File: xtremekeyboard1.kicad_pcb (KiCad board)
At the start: 2 copper layers, 147 x 125.1 mm, 77 parts, among them J2 Conn_01x05_Pin, J3 Conn_01x05_Socket, SW1 1u MX, SW10 1u MX, SW11 1u MX, SW12 1u MX, SW13 1u MX, SW14 1u MX, SW15 1u MX, SW16 1u MX, SW17 1u MX, SW18 1u MX, SW19 1u MX, SW2 1u MX, SW20 1u MX, SW21 1u MX, SW22 1u MX, SW23 1u MX, SW24 1u MX, SW25 1u MX, SW26 1u MX, SW27 1u MX, SW3 1u MX, SW4 1u MX, SW5 1u MX, SW6 1u MX, SW7 1u MX, SW8 1u MX, SW9 1u MX, U1 rp2040-zero, U2 PS4 Joystick

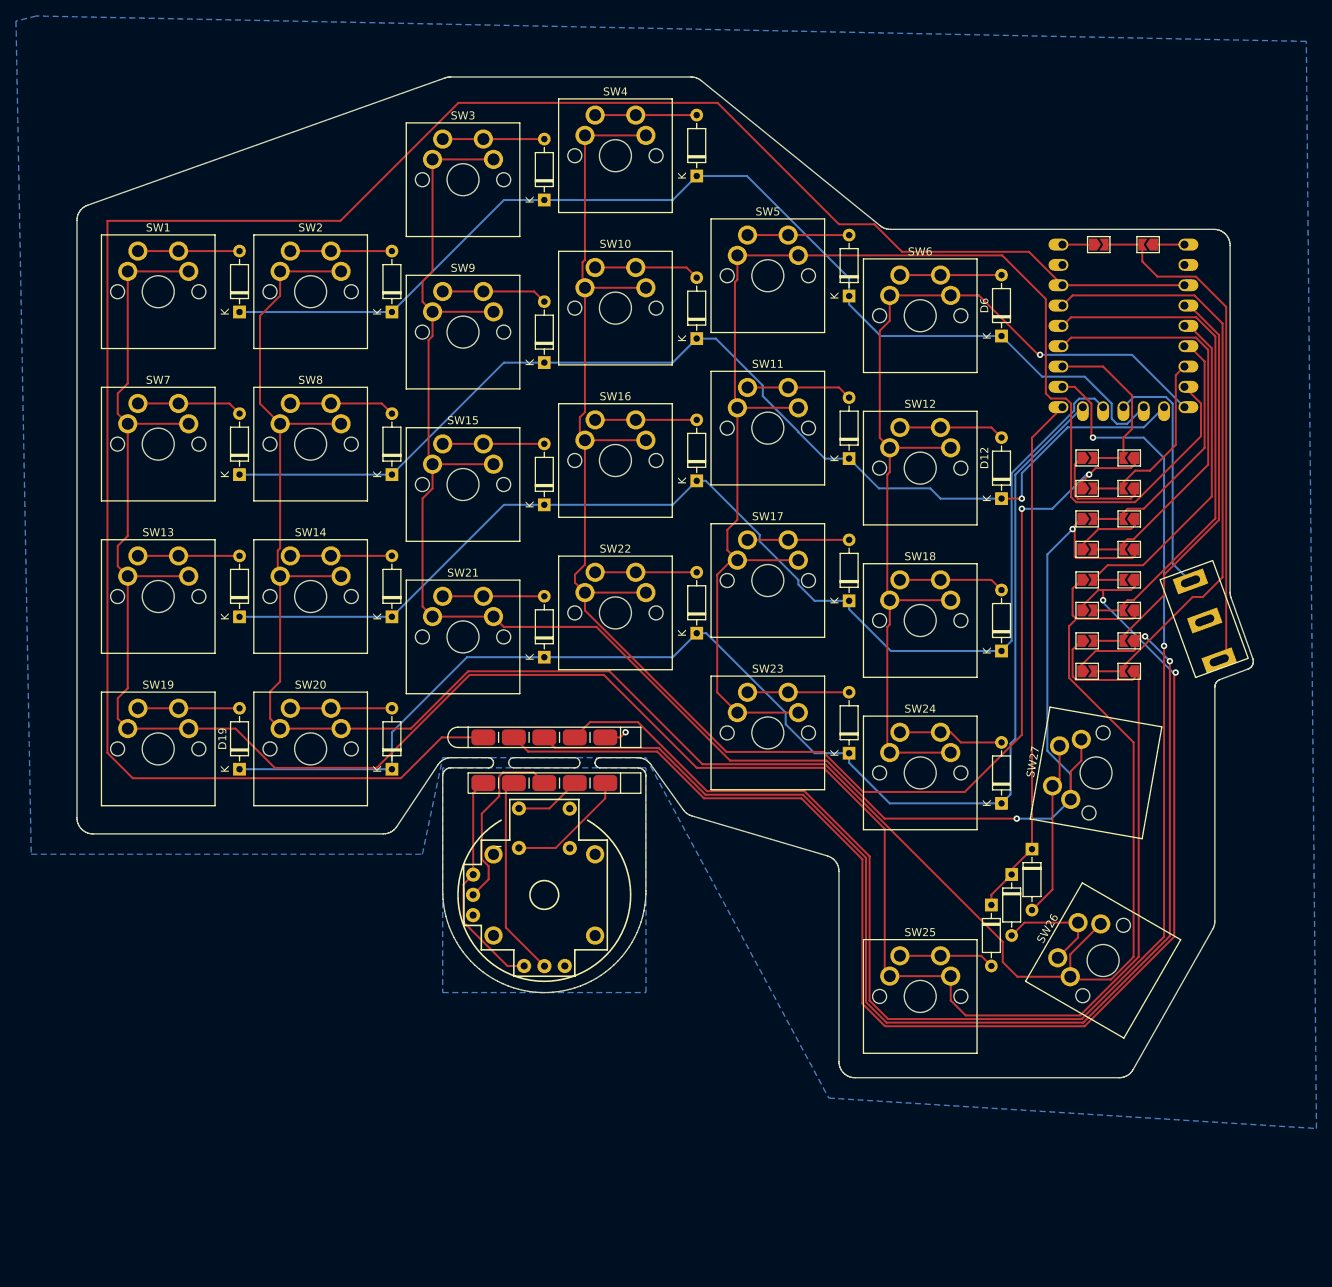
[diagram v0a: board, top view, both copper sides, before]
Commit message: finished pcb routing
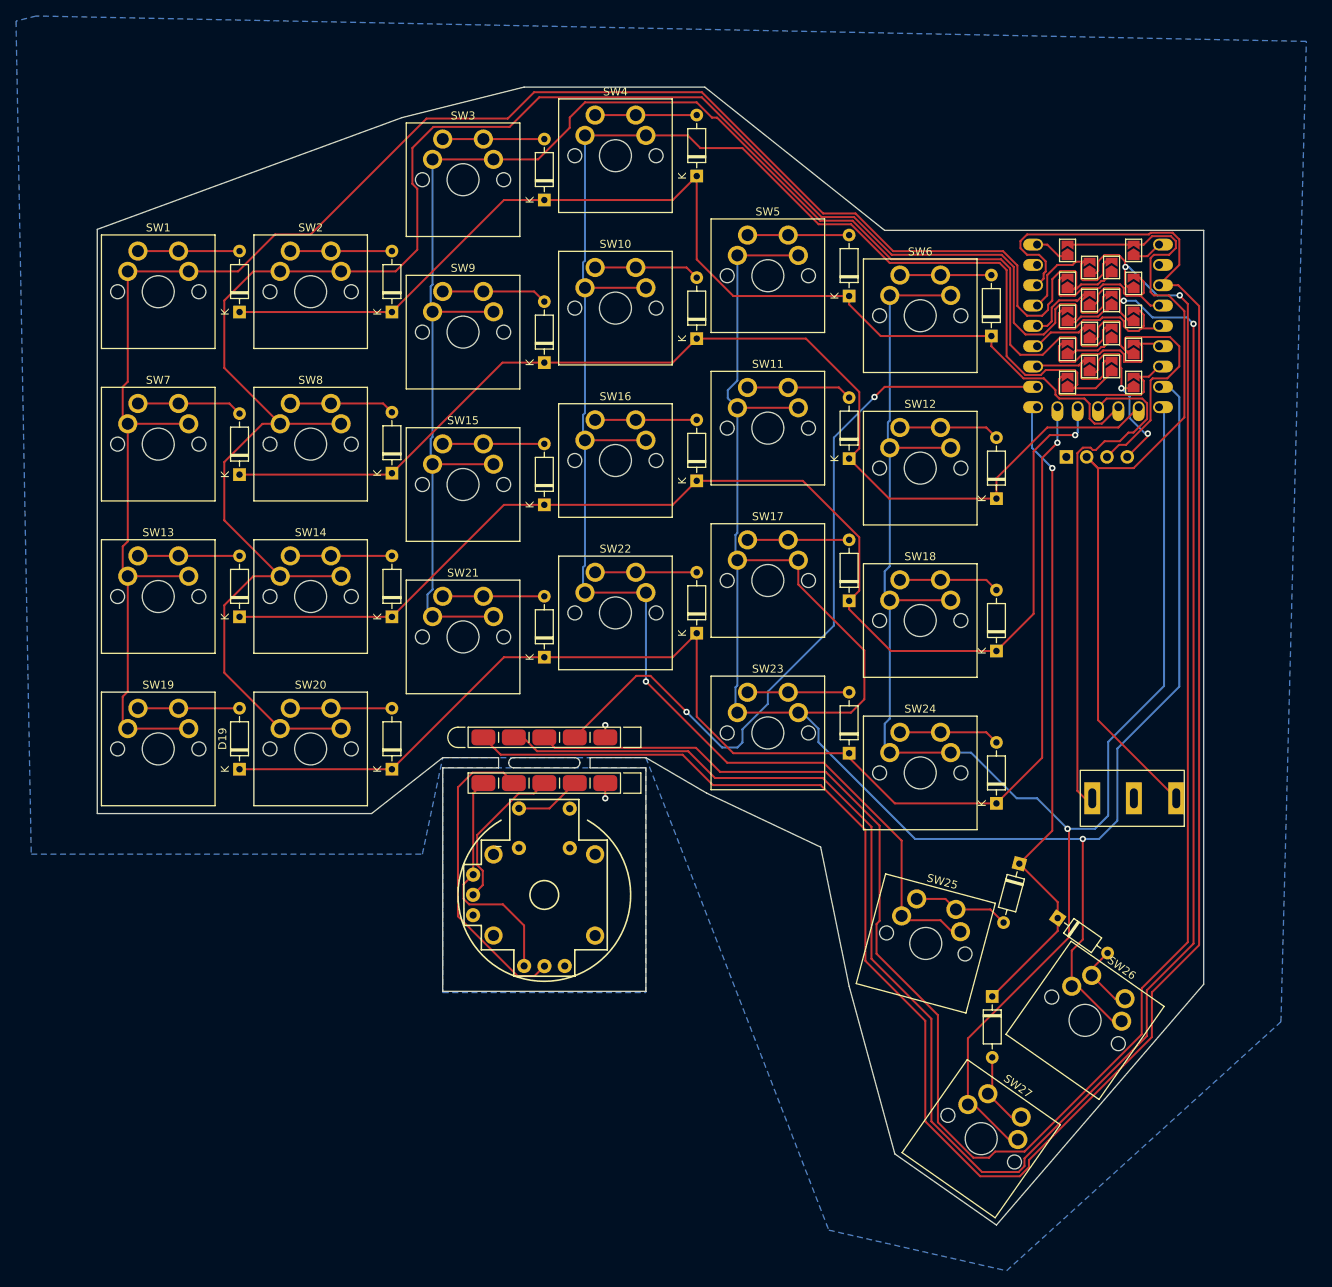
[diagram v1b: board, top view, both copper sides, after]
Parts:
- added J4: OLED-128x32, display:OLED-128x32-cutout, F.Cu at (180.5, 74.5)
- moved JP5 50.5 mm to (176.3, 52.4), turned to 90 degrees
- moved JP4 50.5 mm to (173.6, 52.4), turned to 90 degrees
- moved SW27 47.9 mm to (160.0, 161.3), turned to -35 degrees
- moved JP6 44.7 mm to (170.8, 54.4), turned to 90 degrees
- moved JP3 44.7 mm to (179.1, 54.4), turned to 90 degrees
- moved JP9 38.8 mm to (176.3, 56.5), turned to 90 degrees
- moved JP8 38.7 mm to (173.6, 56.5), turned to 90 degrees
- moved JP10 33.0 mm to (170.8, 58.5), turned to 90 degrees
- moved JP7 32.9 mm to (179.1, 58.5), turned to 90 degrees
- moved JP13 27.1 mm to (176.3, 60.6), turned to 90 degrees
- moved JP12 27.0 mm to (173.6, 60.6), turned to 90 degrees
- moved J1 23.8 mm to (179.2, 118.7), turned to -90 degrees
- moved JP14 21.3 mm to (170.8, 62.6), turned to 90 degrees
- moved JP11 21.2 mm to (179.1, 62.6), turned to 90 degrees
- moved D27 19.1 mm to (161.4, 143.5)
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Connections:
- SW25 pad 1: /COL0 -> /COL3
- SW26 pad 1: /COL1 -> /COL4
- SW27 pad 1: /COL2 -> /COL5
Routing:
- net /COL5: track 124.2 -> 215.2 mm
- net /JOYSW: track 183.2 -> 99.0 mm
- net /JOYY: track 157.6 -> 234.7 mm
- net /COL4: track 178.7 -> 253.4 mm, vias 0 -> 1
- net /JOYX: track 169.0 -> 238.9 mm
- net /COL0: track 298.8 -> 237.6 mm
- net /JYa: track 75.2 -> 18.9 mm
- net /JXa: track 63.8 -> 17.5 mm
- net +5V: track 64.2 -> 103.6 mm
- net /COL2: track 232.1 -> 193.4 mm, vias 2 -> 0
- net /SCLa: track 52.9 -> 15.3 mm
- net /TX: track 30.2 -> 63.1 mm
- net /COL1: track 279.5 -> 247.6 mm
- net /COL3: track 207.5 -> 239.4 mm, vias 2 -> 1
- net /JYb: track 52.8 -> 21.0 mm
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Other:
- board size 147 x 125.1 mm -> 138.3 x 142.2 mm

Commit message: finished good pcb, need to make oled reversible, maybe put jumpers on respective side
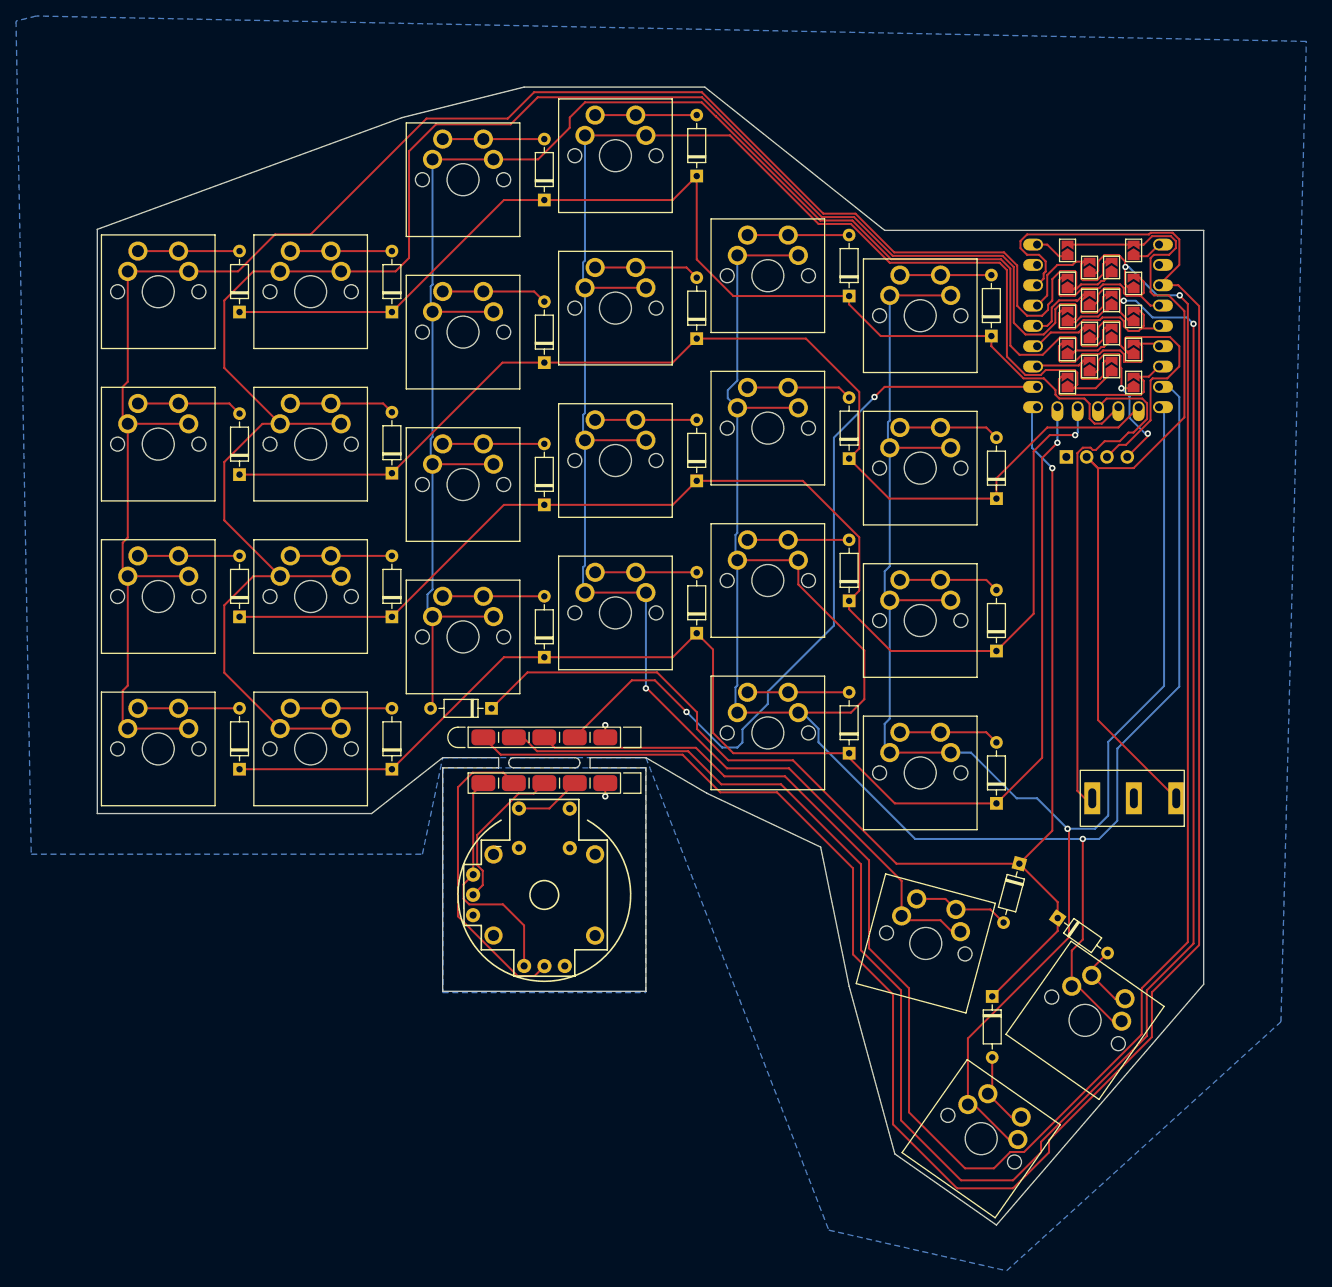
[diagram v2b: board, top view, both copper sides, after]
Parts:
- added D28: 1N4148, Diode_THT:D_DO-35_SOD27_P7.62mm_Horizontal, F.Cu at (98.8, 107.5)
- SW1, SW10, SW11, SW12, SW13, SW14, SW15, SW16, SW17, SW18, SW19, SW2, SW20, SW21, SW22, SW23, SW24, SW25, SW26, SW27, SW3, SW4, SW5, SW6, SW7, SW8, SW9: footprint PCM_Switch_Keyboard_Cherry_MX:SW_Cherry_MX_PCB_1.00u -> PCM_Switch_Keyboard_Cherry_MX:MX_PCB_Reversible
- U1: footprint keyboard_mcu:rp2040-zero-tht -> mcu:rp2040-zero-tht
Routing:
- net /ROW4: track 82.1 -> 161.0 mm
- net /COL2: track 193.4 -> 205.1 mm
- net /COL3: track 239.4 -> 236.9 mm
- net /JOYY: track 234.7 -> 233.5 mm
- net /COL1: track 247.6 -> 247.1 mm

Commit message: added pullup resistors, fixed solder jumpers
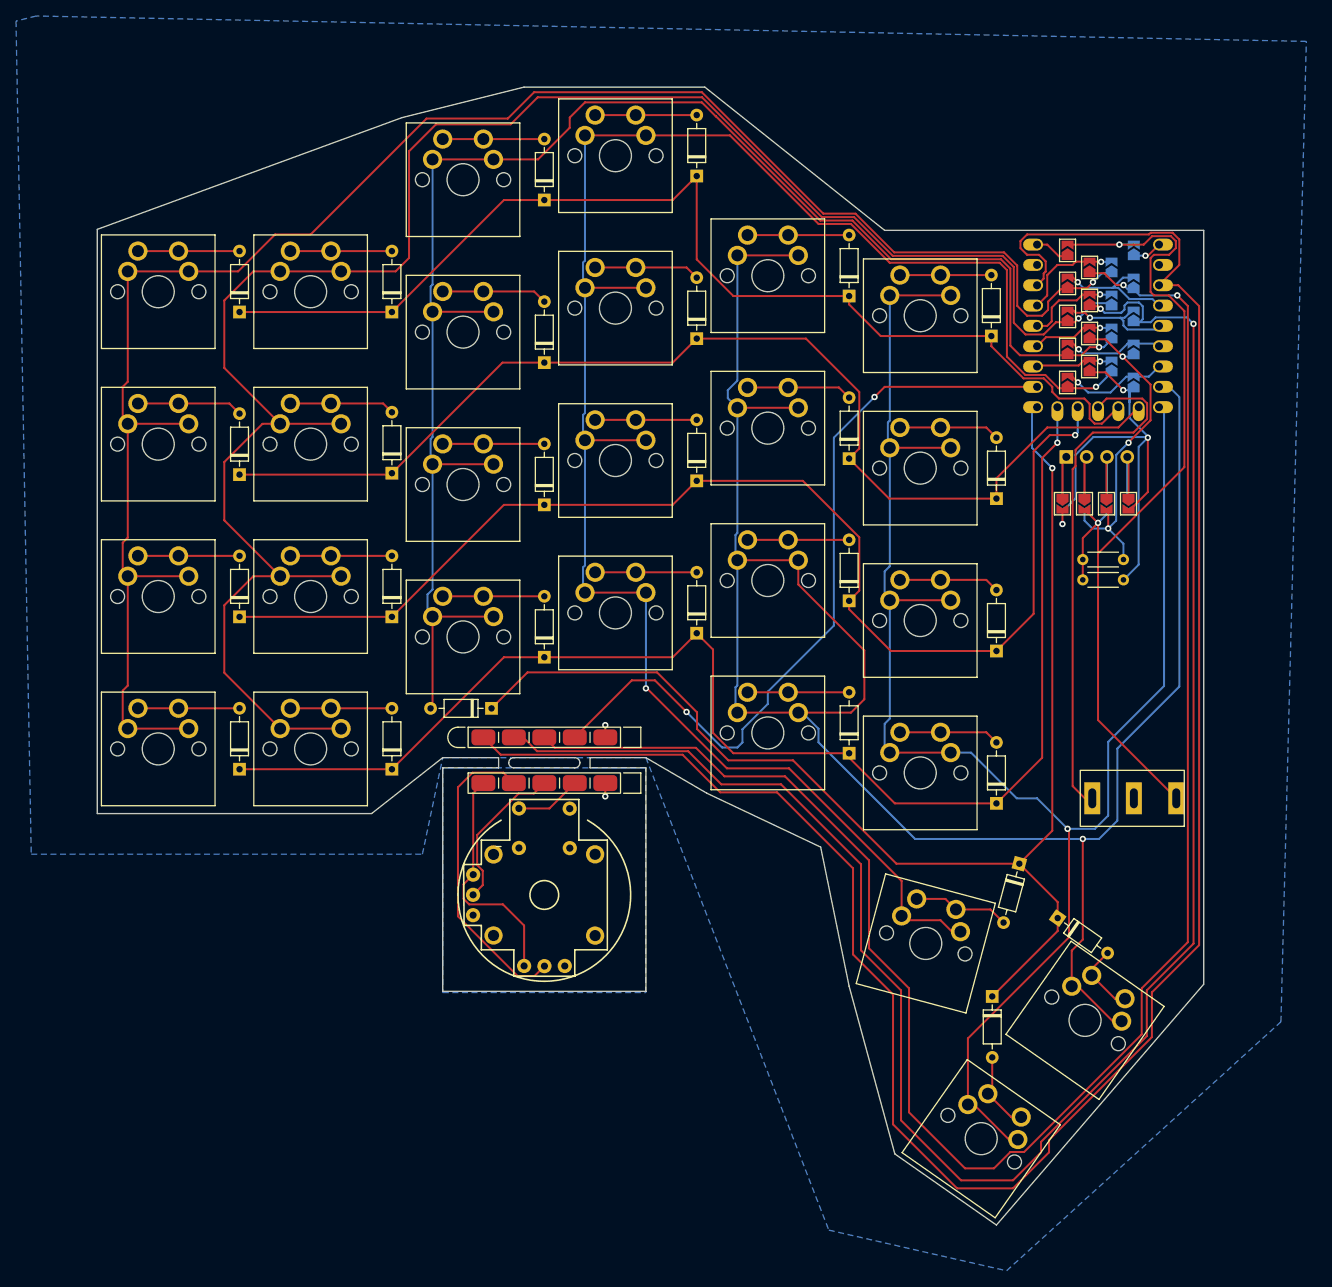
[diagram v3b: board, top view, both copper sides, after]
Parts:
- added JP19: LJumper, Jumper:SolderJumper-2_P1.3mm_Open_TrianglePad1.0x1.5mm, F.Cu at (170.2, 81.9)
- added JP20: RJumper, Jumper:SolderJumper-2_P1.3mm_Open_TrianglePad1.0x1.5mm, B.Cu at (178.4, 81.9)
- added JP21: RJumper, Jumper:SolderJumper-2_P1.3mm_Open_TrianglePad1.0x1.5mm, B.Cu at (170.2, 81.9)
- added JP22: LJumper, Jumper:SolderJumper-2_P1.3mm_Open_TrianglePad1.0x1.5mm, F.Cu at (178.4, 81.9)
- added JP23: LJumper, Jumper:SolderJumper-2_P1.3mm_Open_TrianglePad1.0x1.5mm, F.Cu at (172.9, 81.9)
- added JP24: RJumper, Jumper:SolderJumper-2_P1.3mm_Open_TrianglePad1.0x1.5mm, B.Cu at (175.7, 81.9)
- added JP25: RJumper, Jumper:SolderJumper-2_P1.3mm_Open_TrianglePad1.0x1.5mm, B.Cu at (172.9, 81.9)
- added JP26: LJumper, Jumper:SolderJumper-2_P1.3mm_Open_TrianglePad1.0x1.5mm, F.Cu at (175.7, 81.9)
- added R1: 4.7k, Resistor_THT:R_Axial_DIN0204_L3.6mm_D1.6mm_P5.08mm_Horizontal, F.Cu at (177.8, 88.9)
- added R2: 4.7k, Resistor_THT:R_Axial_DIN0204_L3.6mm_D1.6mm_P5.08mm_Horizontal, F.Cu at (177.8, 91.4)
- JP1, JP11, JP13, JP15, JP17, JP3, JP5, JP7, JP9: moved to B.Cu
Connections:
- J4 pad 1: GND -> /OLED_GND
- J4 pad 2: +5V -> /OLED_VCC
- J4 pad 3: /SCL -> /OLED_SCL
- J4 pad 4: /SDA -> /OLED_SDA
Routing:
- net /SDA: track 22.4 -> 61.5 mm
- net +5V: track 103.6 -> 114.9 mm, vias 0 -> 2
- net /OLED_VCC: track 0.00 -> 10.6 mm
- net /OLED_GND: track 0.00 -> 10.6 mm
- net /OLED_SCL: track 0.00 -> 10.3 mm
- net /OLED_SDA: track 0.00 -> 10.1 mm
- net /SCLb: track 21.6 -> 12.6 mm, vias 0 -> 1
- net /SDAb: track 20.4 -> 13.6 mm, vias 0 -> 1
- net /JOYY: track 233.5 -> 226.9 mm
- net /COL0: track 237.6 -> 231.2 mm, vias 0 -> 1
- net /JXb: track 21.4 -> 15.5 mm, vias 0 -> 1
- net /JYa: track 18.9 -> 13.1 mm, vias 0 -> 1
- net /COL1: track 247.1 -> 241.5 mm, vias 0 -> 1
- net /JXa: track 17.5 -> 12.0 mm, vias 0 -> 1
- net /SDAa: track 14.9 -> 9.69 mm, vias 0 -> 1
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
